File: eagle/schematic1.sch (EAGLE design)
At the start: 32 parts, among them IC1 AD620N, IC2 OP27Z, U7 L7815CV, U8 L7805CV, U9 L7815CV, X1 22-23-2081

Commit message: Fixed MOS package - H and V dim are different - Holes are M4 and not M6
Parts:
- removed LOGO1: JQI-LOGOSILK, JQI_Logo:JQI-LOGOSILK
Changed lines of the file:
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@@
 <part name="GND9" library="supply1" library_urn="urn:adsk.eagle:library:371" deviceset="GND" device=""/>
 <part name="FRAME1" library="frames" library_urn="urn:adsk.eagle:library:229" deviceset="LETTER_L" device=""/>
-<part name="LOGO1" library="JQI_Logo" deviceset="JQI-LOGO" device="SILK"/>
 </parts>
 <sheets>

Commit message: Fixed wrong pinout for negative regulator - This is a classic error that often goes unnoticed. TO2020 Negative regulators have the pinout: 1-GND 2-INPUT 3-OUTPUT This is different from positive regulators with the pinout: 1-INPUT 2-GND 3-OUTPUT Problem fixed. Now the gerbers are ready for production.
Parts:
- U9: value L7815CV -> LM7915; device schematic1:L7815CV -> schematic1:LM7915
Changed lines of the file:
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@@
 <part name="U7" library="schematic1" deviceset="L7815CV" device=""/>
 <part name="U8" library="schematic1" deviceset="L7805CV" device=""/>
-<part name="U9" library="schematic1" deviceset="L7815CV" device=""/>
+<part name="U9" library="schematic1" deviceset="LM7915" device=""/>
 <part name="C6" library="rcl" library_urn="urn:adsk.eagle:library:334" deviceset="C-US" device="025-024X044" package3d_urn="urn:adsk.eagle:package:23630/1"/>
 <part name="P+8" library="supply1" library_urn="urn:adsk.eagle:library:371" deviceset="+15V" device=""/>

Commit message: Removed resistor reordered parts and added LPF
- Resistor from pin 1 and 8 of OP27 is a mistake and it was removed.
- Components name re-ordered and re-assigned
- RC filter added after Teensy DAC. It might be necessary to filter
   out digital interference (especially from USB port)
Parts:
- added C13: (no value), rcl:C-US025-024X044
- C10, C7, C8: device rcl:C-US025-024X044 -> rcl:CPOL-USTT2D4
- C3, C4, C5: device rcl:CPOL-USTT2D4 -> rcl:C-US025-024X044
- IC1: value AD620N -> OP27Z; device schematic1:AD620N -> schematic1:OP27Z
- IC2: value OP27Z -> AD620N; device schematic1:OP27Z -> schematic1:AD620N
- R1: value FHR4V-0R1F1 -> (none); device schematic1:FHR4V-0R1F1 -> rcl:R-US_0204/7
- R7: value (none) -> FHR4V-0R1F1; device rcl:R-US_0204/7 -> schematic1:FHR4V-0R1F1
- renumbered -24V/GND/+24V to JP1, U$1 to T1, U$2 to U1, U$3 to J1, U7 to U2, U8 to U4, U9 to U3
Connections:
- net +15V: now also C1.1, C5.1, IC1.V+, IC2.+V; no longer C6.1, C7.1, IC1.+V, IC2.V+
- net +24V: now also C7.+; no longer C4.+
- net +5V: now also C12.1; no longer C8.1
- net -15V: now also C10.-, C2.2, C6.2, IC1.V-, IC2.-V; no longer C10.2, C12.2, C3.-, IC1.-V, IC2.V-
- net -24V: now also C8.-; no longer C5.-
- net GND: now also C1.2, C10.+, C12.2, C13.2, C2.1, C5.2, C6.1, C7.-, C8.+, IC2.REF, R7.4; no longer C10.1, C12.1, C3.+, C4.-, C5.+, C6.2, C7.2, C8.2, IC1.REF, R1.4
- net N$10: now also R8.2; no longer R4.2
- net N$11: now also C4.2, IC1.OUT, R4.2; no longer C1.2, IC2.OUT, R6.2
- net N$13: now also C3.2, R4.1; no longer C2.2, R6.1
- net N$14: now also C13.1, R3.2, R8.1; no longer IC2.ON1, R7.2
- net N$15: now also IC1.ON2; no longer IC2.ON2, R7.1
- net N$17: now also R7.1; no longer R1.1
- net N$18: now also IC2.+, R7.2; no longer IC1.+, R1.2
- net N$19: now also IC2.-, R7.3; no longer IC1.-, R1.3
- net N$3: now also R1.1; no longer R8.1
- net N$4: now also IC2.RG@1, R6.2; no longer IC1.RG@1, R2.2
- net N$5: now also IC2.RG@2, R6.1; no longer IC1.RG@2, R2.1
- net N$7: now also IC2.OUT, R1.2, R2.2; no longer IC1.OUT, R3.2, R8.2
- net N$8: now also C3.1, C4.1, IC1.-IN, R2.1; no longer C1.1, C2.1, IC2.-IN, R3.1
- net N$9: now also IC1.+IN, R3.1; no longer IC2.+IN, R4.1

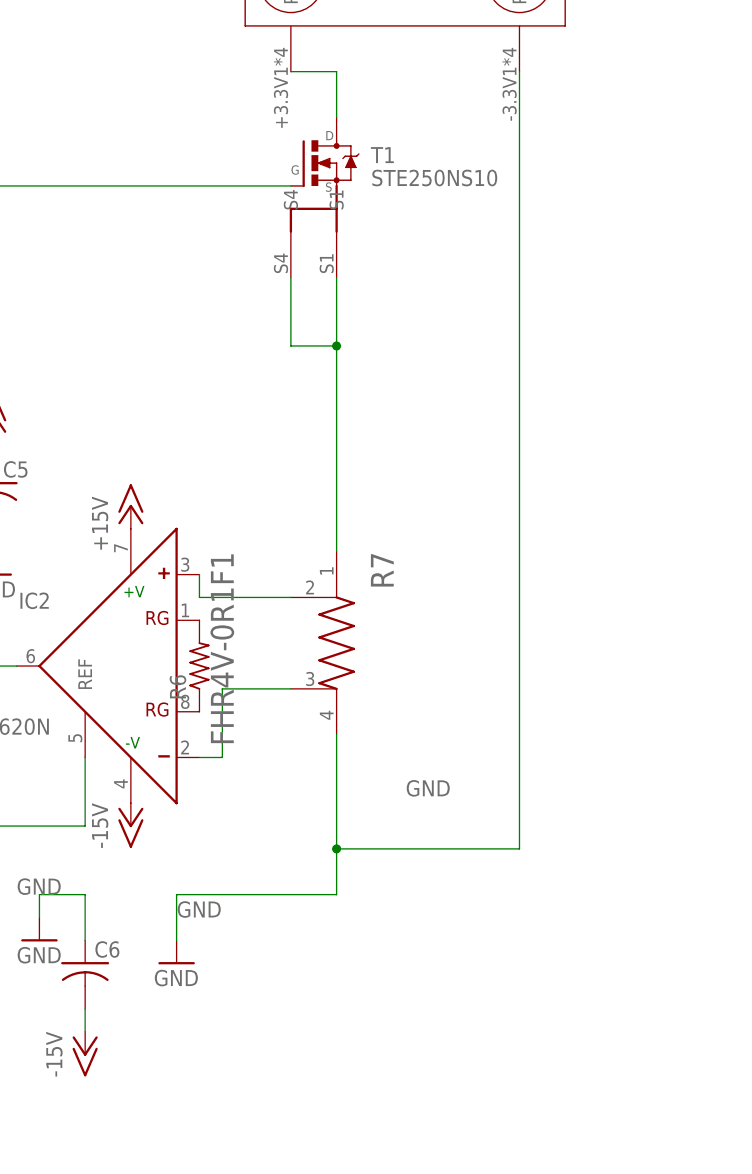
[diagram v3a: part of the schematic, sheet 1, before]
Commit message: Changed value of sensing resistor to 0.01Ohm and added value for R6 TO DO:   1 - Add missing values for resistors and capacitors according with the prototype board   2 - Fix the hole size  for the large   3 - Update gerber zip file to reflect change in hole size.
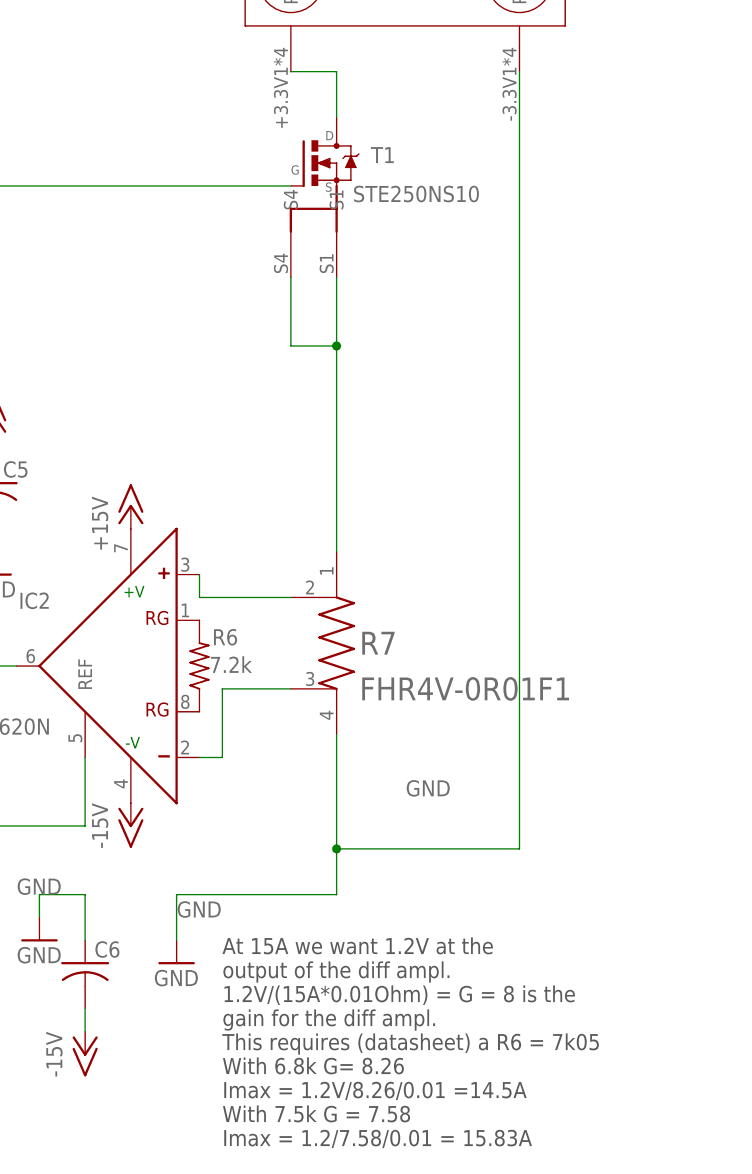
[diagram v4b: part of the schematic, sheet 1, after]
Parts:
- R6: value (none) -> 7.2k
- R7: value FHR4V-0R1F1 -> FHR4V-0R01F1
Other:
- note added: "At 15A we want 1.2V at the output of the diff ampl. 1.2V/(15A*0.01Ohm) = G = 8 is the gain for the diff ampl. This requires (datasheet) a R6 = 7k05 With 6.8k G= 8.26 Imax = 1.2V/8.26/0.01 =14.5A With 7.5k G = 7.58 Imax = 1.2/7.58/0.01 = 15.83A"
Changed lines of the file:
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@@
 <parts>
 <part name="IC2" library="schematic1" deviceset="AD620" device="N"/>
-<part name="R6" library="rcl" library_urn="urn:adsk.eagle:library:334" deviceset="R-US_" device="0204/7" package3d_urn="urn:adsk.eagle:package:23498/2"/>
+<part name="R6" library="rcl" library_urn="urn:adsk.eagle:library:334" deviceset="R-US_" device="0204/7" package3d_urn="urn:adsk.eagle:package:23498/2" value="7.2k"/>
 <part name="R2" library="rcl" library_urn="urn:adsk.eagle:library:334" deviceset="R-US_" device="0204/7" package3d_urn="urn:adsk.eagle:package:23498/2"/>
 <part name="IC1" library="schematic1" deviceset="OP27" device="Z"/>
@@
 <part name="C12" library="rcl" library_urn="urn:adsk.eagle:library:334" deviceset="C-US" device="025-024X044" package3d_urn="urn:adsk.eagle:package:23630/1"/>
 <part name="P+9" library="supply1" library_urn="urn:adsk.eagle:library:371" deviceset="+5V" device=""/>
-<part name="R7" library="schematic1" deviceset="FHR4V-0R1F1" device=""/>
+<part name="R7" library="schematic1" deviceset="FHR4V-0R1F1" device="" value="FHR4V-0R01F1"/>
 <part name="P+1" library="supply1" library_urn="urn:adsk.eagle:library:371" deviceset="+5V" device=""/>
 <part name="T1" library="schematic1" deviceset="STE250NS10" device=""/>
@@
 <sheet>
 <plain>
+<text x="205.74" y="30.48" size="1.778" layer="97">At 15A we want 1.2V at the
+output of the diff ampl.
+1.2V/(15A*0.01Ohm) = G = 8 is the
+gain for the diff ampl.
+This requires (datasheet) a R6 = 7k05
+With 6.8k G= 8.26
+Imax = 1.2V/8.26/0.01 =14.5A
+With 7.5k G = 7.58
+Imax = 1.2/7.58/0.01 = 15.83A
+</text>
 </plain>
 <instances>
@@
 </instance>
 <instance part="R6" gate="G$1" x="203.2" y="83.82" smashed="yes" rot="R90">
-<attribute name="NAME" x="201.7014" y="80.01" size="1.778" layer="95" rot="R90"/>
-<attribute name="VALUE" x="206.502" y="80.01" size="1.778" layer="96" rot="R90"/>
+<attribute name="NAME" x="207.518" y="87.9094" size="1.778" layer="95" rot="R180"/>
+<attribute name="VALUE" x="209.042" y="84.836" size="1.778" layer="96" rot="R180"/>
 </instance>
 <instance part="R2" gate="G$1" x="129.54" y="134.62" smashed="yes" rot="R180">
@@
 </instance>
 <instance part="R7" gate="G$1" x="218.44" y="86.36" smashed="yes" rot="R270">
-<attribute name="NAME" x="222.25" y="96.52" size="2.54" layer="95" rot="R270"/>
-<attribute name="VALUE" x="204.47" y="96.52" size="2.54" layer="96" rot="R270"/>
+<attribute name="NAME" x="220.98" y="85.09" size="2.54" layer="95"/>
+<attribute name="VALUE" x="220.98" y="80.01" size="2.54" layer="96"/>
 </instance>
 <instance part="P+1" gate="1" x="99.06" y="172.72" smashed="yes">
@@
 <instance part="T1" gate="MOSFET" x="218.44" y="139.7" smashed="yes">
 <attribute name="NAME" x="222.258140625" y="139.7" size="1.78028125" layer="95"/>
-<attribute name="VALUE" x="222.262590625" y="137.15496875" size="1.78151875" layer="96"/>
+<attribute name="VALUE" x="220.230590625" y="135.37696875" size="1.78151875" layer="96"/>
 </instance>
 <instance part="C1" gate="G$1" x="129.54" y="157.48" smashed="yes">
@@
 </drawing>
 <compatibility>
+<note version="6.3" minversion="6.2.2" severity="warning">
+Since Version 6.2.2 text objects can contain more than one line,
+which will not be processed correctly with this version.
+</note>
 <note version="8.2" severity="warning">
 Since Version 8.2, EAGLE supports online libraries. The ids
